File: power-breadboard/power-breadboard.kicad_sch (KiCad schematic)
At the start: 0 parts

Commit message: power-pcb: add imd input to safety systems page
Use the same CAN transceiver as for the network since it also supports
24V-CAN. Also re-added a separate 24V input for the contactors.
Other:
- sheet Relay Board Connections ports: added CONTACTORS_24V; removed none
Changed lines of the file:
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@@
 	(sheet
 		(at 157.48 46.99)
-		(size 40.64 35.56)
+		(size 40.64 41.91)
 		(exclude_from_sim no)
 		(in_bom yes)
@@
 		)
 		(property "Sheetfile" "relay_board_connections.kicad_sch"
-			(at 157.48 83.1346 0)
+			(at 157.48 89.4846 0)
 			(show_name no)
 			(do_not_autoplace no)
@@
 			(effects
 				(font
+					(size 1.27 1.27)
+				)
+				(justify left)
+			)
+		)
+		(pin "CONTACTORS_24V" input
+			(at 157.48 86.36 180)
+			(effects
+				(font

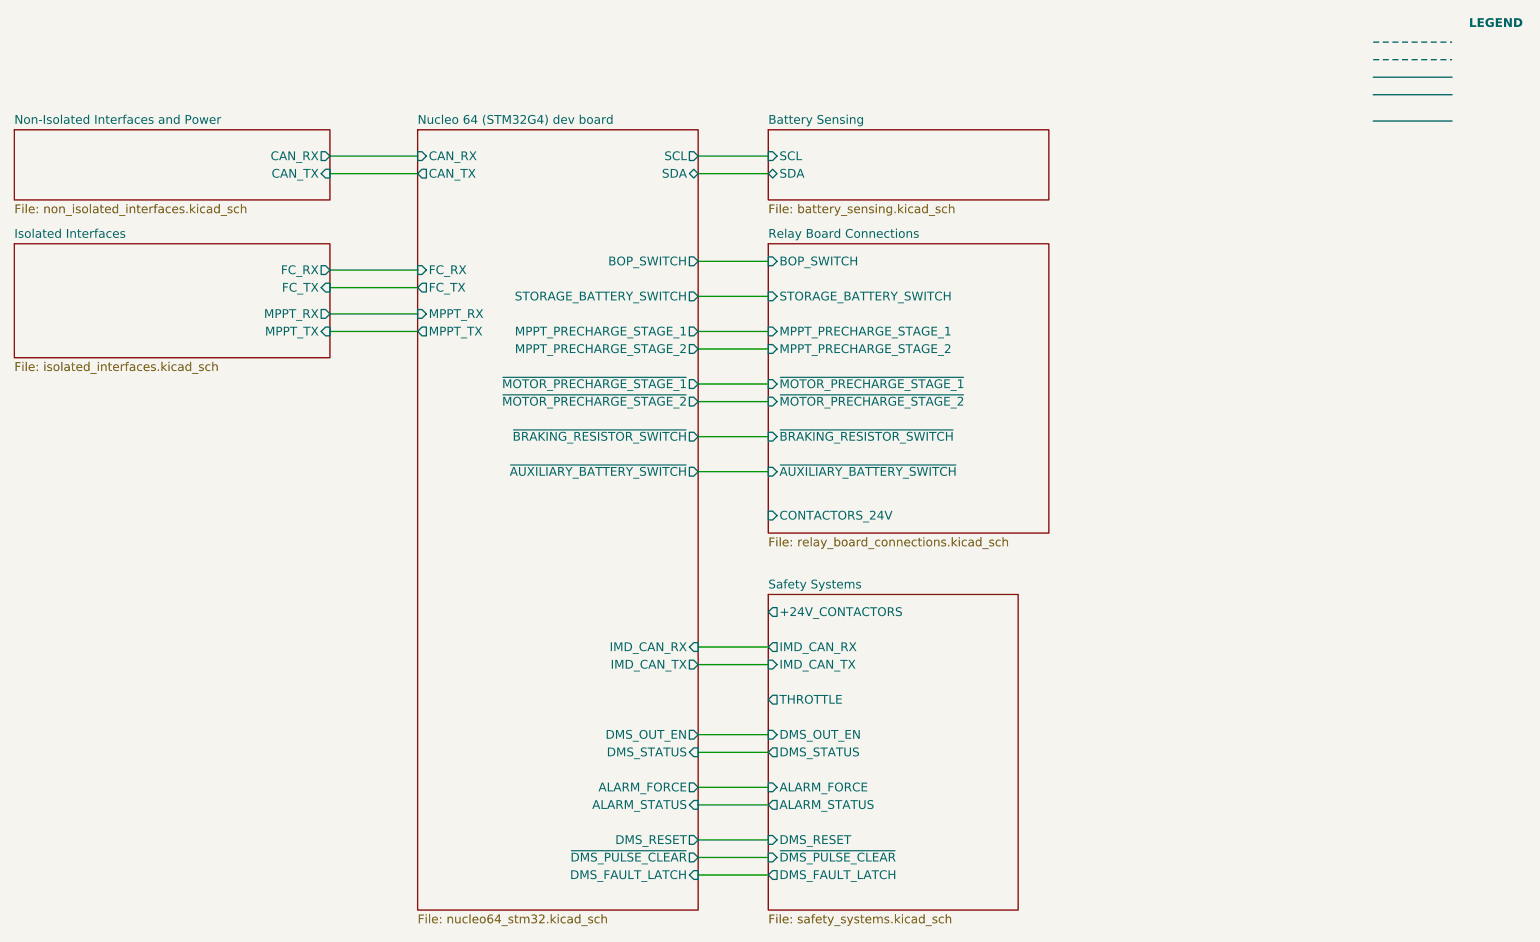
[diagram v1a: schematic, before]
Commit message: power-breadboard: complete nucleo peripheral table
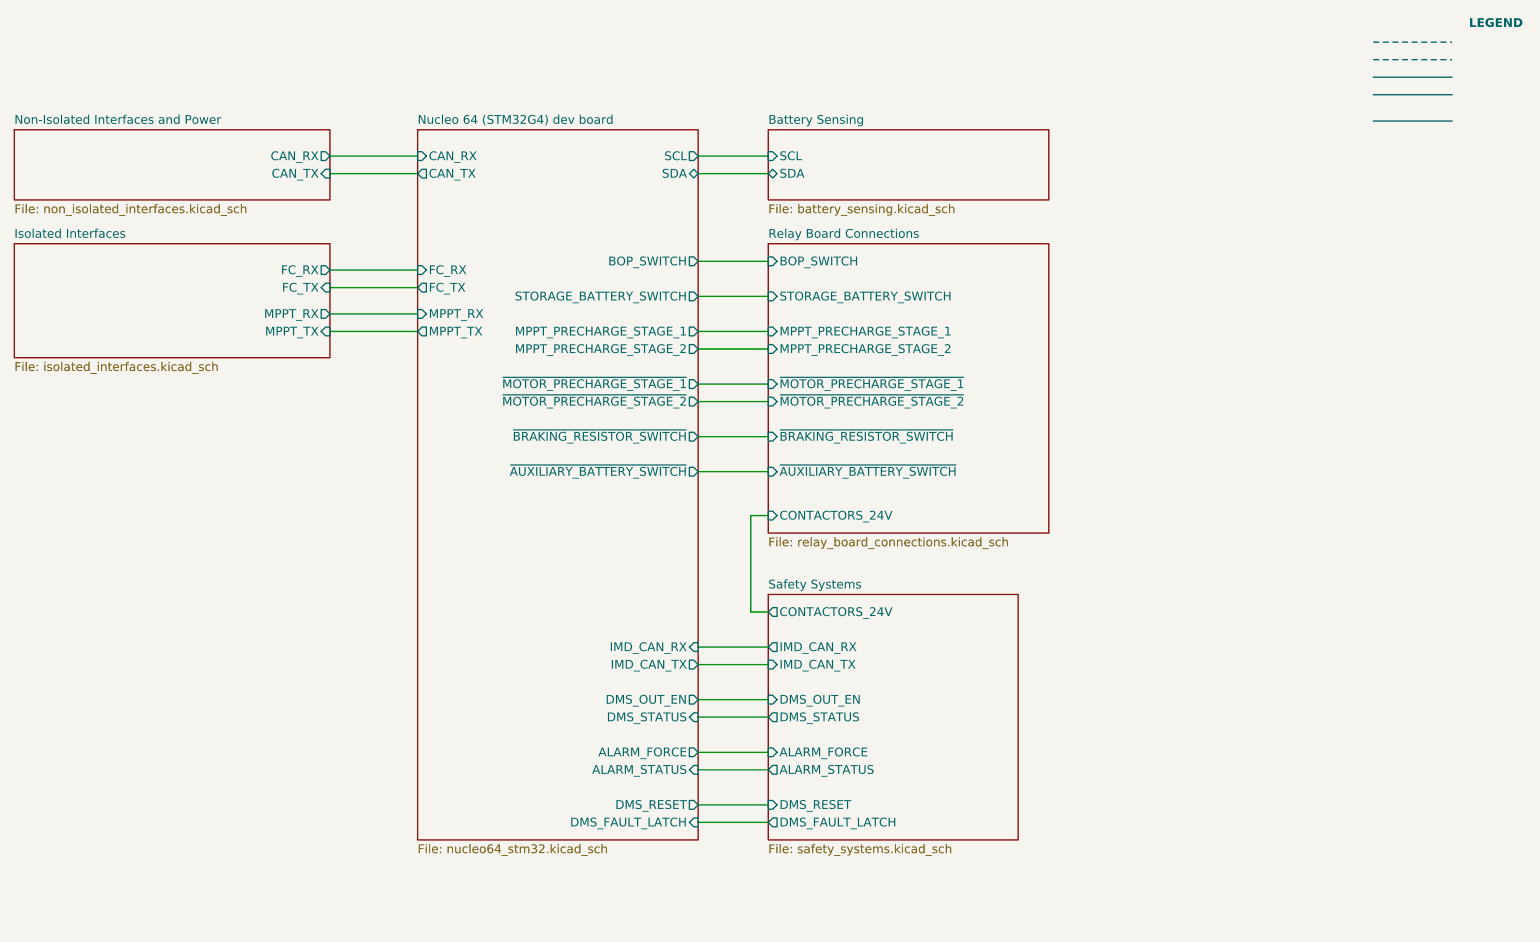
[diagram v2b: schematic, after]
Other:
- sheet Nucleo 64 (STM32G4) dev board ports: added none; removed ~{DMS_PULSE_CLEAR}
- sheet Safety Systems ports: added CONTACTORS_24V; removed +24V_CONTACTORS, THROTTLE, ~{DMS_PULSE_CLEAR}
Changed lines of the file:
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@@
 	(title_block
 		(title "Overview")
-		(date "2026-06-29")
+		(date "2026-07-01")
 		(rev "v1.1.0")
 	)
@@
 	(wire
 		(pts
-			(xy 147.32 118.11) (xy 157.48 118.11)
-		)
-		(stroke
-			(width 0)
-			(type default)
+			(xy 147.32 113.03) (xy 157.48 113.03)
+		)
+		(stroke
+			(width 0)
+			(type default)
+		)
+	)
+	(wire
+		(pts
+			(xy 154.94 100.33) (xy 157.48 100.33)
+		)
+		(stroke
+			(width 0)
+			(type default)
+			(color 194 0 194 1)
 		)
 	)
@@
 	(wire
 		(pts
-			(xy 147.32 138.43) (xy 157.48 138.43)
+			(xy 147.32 130.81) (xy 157.48 130.81)
 		)
 		(stroke
@@
 	(wire
 		(pts
+			(xy 147.32 115.57) (xy 157.48 115.57)
+		)
+		(stroke
+			(width 0)
+			(type default)
+		)
+	)
+	(wire
+		(pts
+			(xy 147.32 105.41) (xy 157.48 105.41)
+		)
+		(stroke
+			(width 0)
+			(type default)
+		)
+	)
+	(wire
+		(pts
+			(xy 147.32 123.19) (xy 157.48 123.19)
+		)
+		(stroke
+			(width 0)
+			(type default)
+		)
+	)
+	(wire
+		(pts
+			(xy 147.32 62.23) (xy 157.48 62.23)
+		)
+		(stroke
+			(width 0)
+			(type default)
+		)
+	)
+	(wire
+		(pts
+			(xy 154.94 86.36) (xy 154.94 100.33)
+		)
+		(stroke
+			(width 0)
+			(type default)
+			(color 194 0 194 1)
+		)
+	)
+	(wire
+		(pts
+			(xy 157.48 86.36) (xy 154.94 86.36)
+		)
+		(stroke
+			(width 0)
+			(type default)
+			(color 194 0 194 1)
+		)
+	)
+	(wire
+		(pts
 			(xy 147.32 120.65) (xy 157.48 120.65)
 		)
@@
 	(wire
 		(pts
-			(xy 147.32 105.41) (xy 157.48 105.41)
+			(xy 147.32 59.69) (xy 157.48 59.69)
 		)
 		(stroke
@@
 		(pts
 			(xy 147.32 128.27) (xy 157.48 128.27)
-		)
-		(stroke
-			(width 0)
-			(type default)
-		)
-	)
-	(wire
-		(pts
-			(xy 147.32 135.89) (xy 157.48 135.89)
-		)
-		(stroke
-			(width 0)
-			(type default)
-		)
-	)
-	(wire
-		(pts
-			(xy 147.32 62.23) (xy 157.48 62.23)
-		)
-		(stroke
-			(width 0)
-			(type default)
-		)
-	)
-	(wire
-		(pts
-			(xy 147.32 125.73) (xy 157.48 125.73)
-		)
-		(stroke
-			(width 0)
-			(type default)
-		)
-	)
-	(wire
-		(pts
-			(xy 147.32 59.69) (xy 157.48 59.69)
-		)
-		(stroke
-			(width 0)
-			(type default)
-		)
-	)
-	(wire
-		(pts
-			(xy 147.32 133.35) (xy 157.48 133.35)
 		)
 		(stroke
@@
 	(sheet
 		(at 157.48 97.79)
-		(size 36.195 45.72)
+		(size 36.195 35.56)
 		(exclude_from_sim no)
 		(in_bom yes)
@@
 		)
 		(property "Sheetfile" "safety_systems.kicad_sch"
-			(at 157.48 144.0946 0)
+			(at 157.48 133.9346 0)
 			(show_name no)
 			(do_not_autoplace no)
@@
 		)
 		(pin "DMS_STATUS" output
+			(at 157.48 115.57 180)
+			(effects
+				(font
+					(size 1.27 1.27)
+				)
+				(justify left)
+			)
+		)
+		(pin "ALARM_FORCE" input
 			(at 157.48 120.65 180)
 			(effects
@@
 			)
 		)
-		(pin "THROTTLE" output
-			(at 157.48 113.03 180)
-			(effects
-				(font
-					(size 1.27 1.27)
-				)
-				(justify left)
-			)
-		)
-		(pin "+24V_CONTACTORS" output
-			(at 157.48 100.33 180)
-			(effects
-				(font
-					(size 1.27 1.27)
-				)
-				(justify left)
-			)
-		)
-		(pin "ALARM_FORCE" input
-			(at 157.48 125.73 180)
-			(effects
-				(font
-					(size 1.27 1.27)
-				)
-				(justify left)
-			)
-		)
 		(pin "ALARM_STATUS" output
-			(at 157.48 128.27 180)
+			(at 157.48 123.19 180)
 			(effects
 				(font
@@
 		)
 		(pin "DMS_OUT_EN" input
-			(at 157.48 118.11 180)
+			(at 157.48 113.03 180)
 			(effects
 				(font
@@
 		)
 		(pin "DMS_RESET" input
-			(at 157.48 133.35 180)
-			(effects
-				(font
-					(size 1.27 1.27)
-				)
-				(justify left)
-			)
-		)
-		(pin "~{DMS_PULSE_CLEAR}" input
-			(at 157.48 135.89 180)
+			(at 157.48 128.27 180)
 			(effects
 				(font
@@
 		)
 		(pin "DMS_FAULT_LATCH" output
-			(at 157.48 138.43 180)
+			(at 157.48 130.81 180)
+			(effects
+				(font
+					(size 1.27 1.27)
+				)
+				(justify left)
+			)
+		)
+		(pin "CONTACTORS_24V" output
+			(at 157.48 100.33 180)
 			(effects
 				(font
@@
 	(sheet
 		(at 106.68 30.48)
-		(size 40.64 113.03)
+		(size 40.64 102.87)
 		(exclude_from_sim no)
 		(in_bom yes)
@@
 		)
 		(property "Sheetfile" "nucleo64_stm32.kicad_sch"
-			(at 106.68 144.0946 0)
+			(at 106.68 133.9346 0)
 			(show_name no)
 			(do_not_autoplace no)
@@
 		)
 		(pin "ALARM_FORCE" output
-			(at 147.32 125.73 0)
+			(at 147.32 120.65 0)
 			(effects
 				(font
@@
 		)
 		(pin "ALARM_STATUS" input
-			(at 147.32 128.27 0)
+			(at 147.32 123.19 0)
 			(effects
 				(font
@@
 		)
 		(pin "DMS_STATUS" input
-			(at 147.32 120.65 0)
+			(at 147.32 115.57 0)
 			(effects
 				(font
@@
 		)
 		(pin "DMS_OUT_EN" output
-			(at 147.32 118.11 0)
+			(at 147.32 113.03 0)
 			(effects
 				(font
@@
 		)
 		(pin "DMS_RESET" output
-			(at 147.32 133.35 0)
-			(effects
-				(font
-					(size 1.27 1.27)
-				)
-				(justify right)
-			)
-		)
-		(pin "~{DMS_PULSE_CLEAR}" output
-			(at 147.32 135.89 0)
+			(at 147.32 128.27 0)
 			(effects
 				(font
@@
 		)
 		(pin "DMS_FAULT_LATCH" input
-			(at 147.32 138.43 0)
-			(effects
-				(font
+			(at 147.32 130.81 0)
+			(effects
+				(font
